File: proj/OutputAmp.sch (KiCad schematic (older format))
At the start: 0 parts

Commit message: Add output amplifier schematic
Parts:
- added C? (x4): 100n, IPC7351-Nominal:CAPC2012X70, symbol C-0805
- added C? (x6): 1n, IPC7351-Nominal:CAPC1005X55, symbol C-0402
- added C? (x2): 10u, IPC7351-Nominal:CAPC2012X70, symbol C-0805
- added C? (x2): 10u, IPC7351-Nominal:CAPC3216X70, symbol C-1206
- added Q? (x2): 2N7002, smd-semi:SOT-23, symbol 2N7002
- added Q?: MMBT3906, smd-semi:SOT-23, symbol MMBT3906
- added R?: 180, IPC7351-Nominal:RESC1005X40, symbol R-0402
- added R?: 36, IPC7351-Nominal:RESC1005X40, symbol R-0402
- added R?: 49R9, IPC7351-Nominal:RESC1005X40, symbol R-0402
- added R?: 750, IPC7351-Nominal:RESC1005X40, symbol R-0402
- added R?: 150, IPC7351-Nominal:RESC1005X40, symbol R-0402
- added R? (x6): 33, IPC7351-Nominal:RESC1608X50, symbol R-0603
- added R? (x2): 220, IPC7351-Nominal:RESC1005X40, symbol R-0402
- added R? (x3): 1k, IPC7351-Nominal:RESC1005X40, symbol R-0402
- added R?: 10k, IPC7351-Nominal:RESC1005X40, symbol R-0402
- added U?: MAADSS0008, smd-semi:SOT-23-5, symbol MAADSS0008
- added U? (x2): AD8000YRDZ, IPC7351-Nominal:SOIC127P600X175-9, symbol AD8000YRDZ
- added U? (x2): THS3001IDGN, IPC7351-Nominal:SOP65P490X110-9A, symbol THS3001IDGN
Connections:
- new net: C?.1, R?.1, U?.4 (BIAS1)
- new net: C?.1, R?.1, U?.5 (BIAS2)
- new net: R?.1, U?.1
- new net: R?.1, R?.2, U?.2 (x2)
- new net: U?.3, U?.6
- new net: R?.1, R?.2, R?.2, U?.6
- new net: R?.1, R?.1, R?.2, R?.2 (x2)
- new net: Q?.1, Q?.3, R?.2, R?.2
- new net: Q?.3, R?.2, R?.2
- new net: Q?.1, Q?.3, R?.1
- new net: Q?.2, R?.2
- new net +5: C?.1, C?.1, C?.1, U?.7 (+VS), U?.8 (#SHDN)
- new net +9: C?.1, C?.1, C?.1, U?.7 (V+)
- new net -5: C?.2, C?.2, C?.2, Q?.2, Q?.2, R?.2, U?.4 (-VS)
- new net -9: C?.2, C?.2, C?.2, U?.4 (V-), U?.9 (PAD)
- new net ATTEN: R?.1
- new net GND: C?.1, C?.1, C?.1, C?.1, C?.1, C?.1, C?.2, C?.2, C?.2, C?.2, C?.2, C?.2, C?.2, C?.2, Q?.1, R?.1, R?.1, R?.2, R?.2, R?.2, U?.9 (PAD)
- new net INPUT: U?.1 (IN)
- new net LPF/A: U?.3 (OUT)
- new net LPF/B: R?.1, U?.3
- new net OUT: R?.1, R?.1

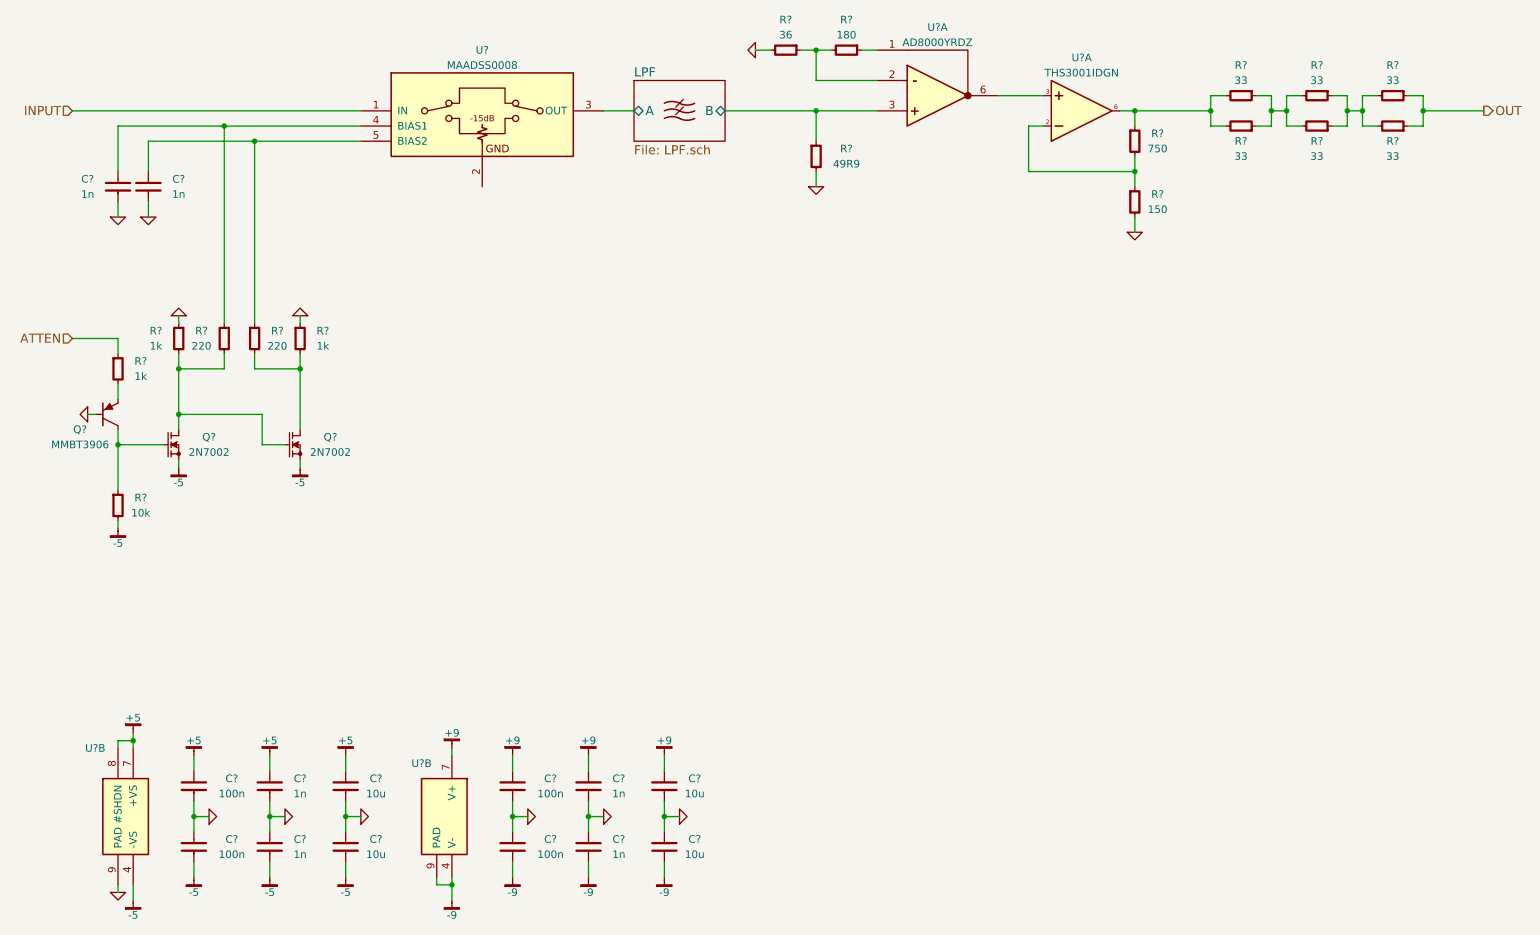
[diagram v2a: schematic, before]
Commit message: Add power input circuit
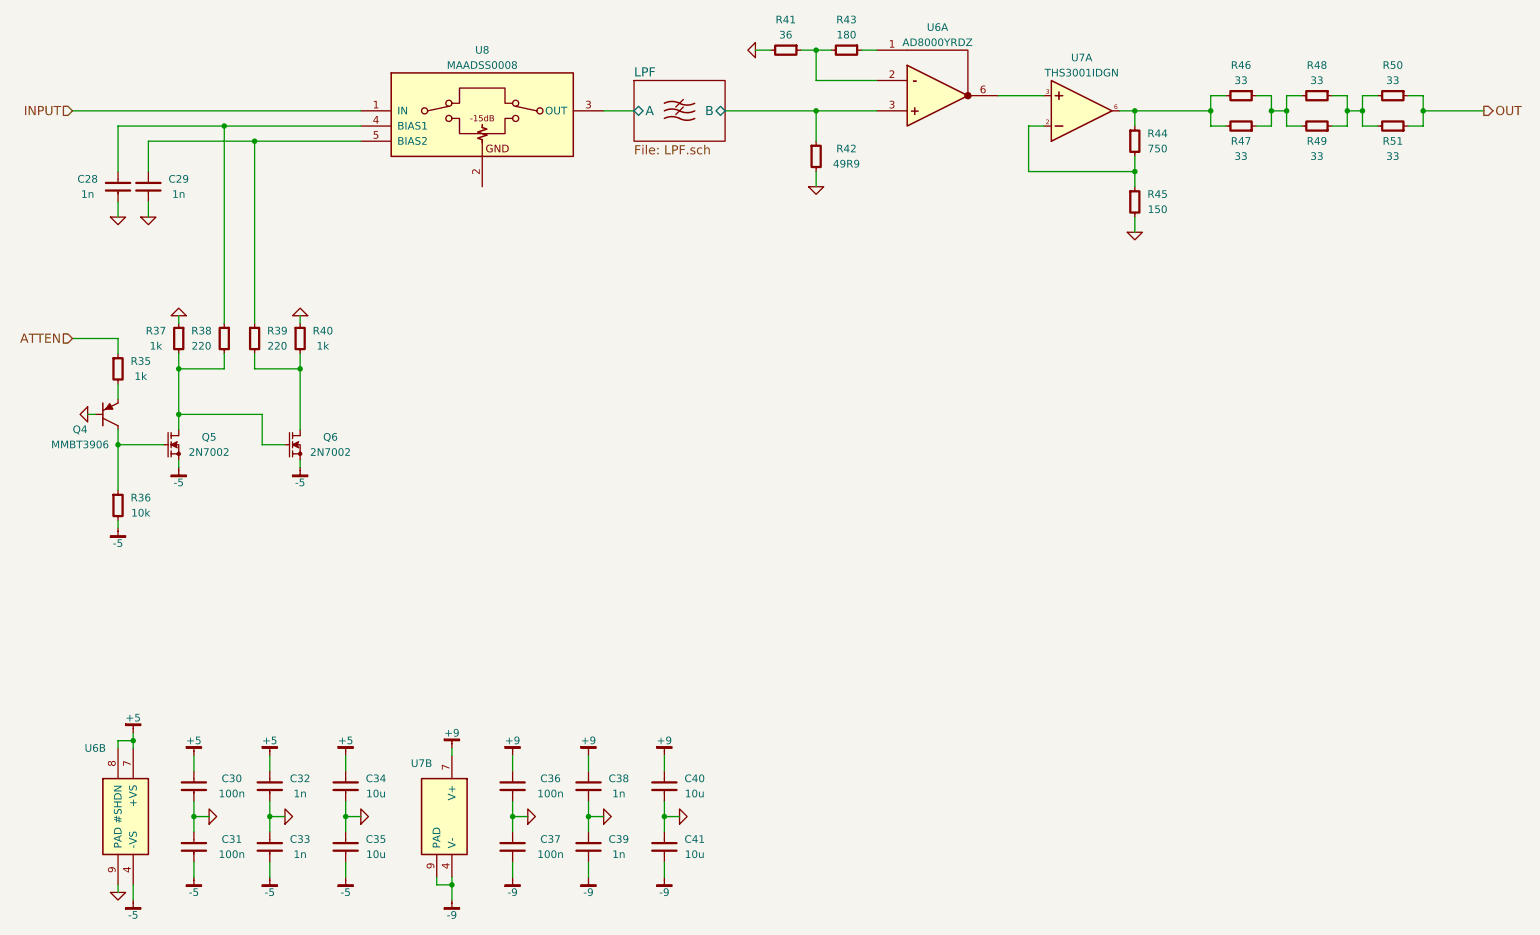
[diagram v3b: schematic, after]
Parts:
- gave numbers to parts that had none: 37

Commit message: Layout most analog bits
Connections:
- net GND: now also U8.2
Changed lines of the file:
@@
 Wire Wire Line
 	1800 3500 1500 3500
+$Comp
+L GND #PWR0155
+U 1 1 54F7DEC8
+P 4200 2550
+F 0 "#PWR0155" H 4200 2550 30  0001 C CNN
+F 1 "GND" H 4200 2480 30  0001 C CNN
+F 2 "" H 4200 2550 60  0000 C CNN
+F 3 "" H 4200 2550 60  0000 C CNN
+	1    4200 2550
+	1    0    0    -1
+$EndComp
+Wire Wire Line
+	4200 2550 4200 2500
 $EndSCHEMATC
